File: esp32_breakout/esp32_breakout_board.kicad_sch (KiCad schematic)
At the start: 12 parts, among them U4 ESP32-S3-MINI-1

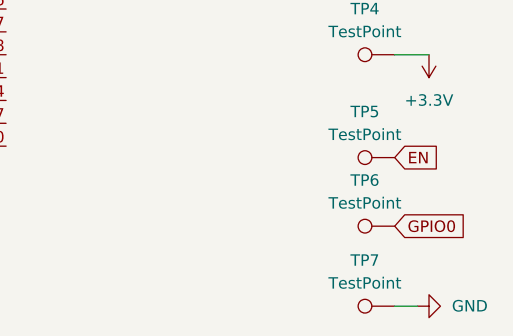
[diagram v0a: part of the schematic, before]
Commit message: Updated esp32 breakout board
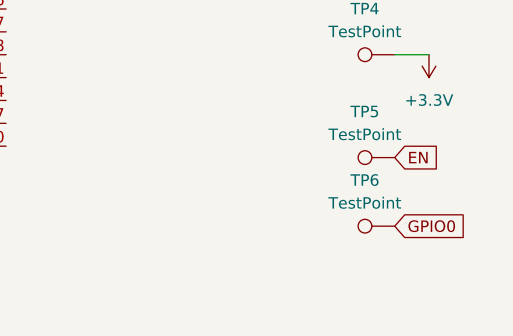
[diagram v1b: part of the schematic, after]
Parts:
- removed TP7: TestPoint, TestPoint:TestPoint_THTPad_D2.0mm_Drill1.0mm, symbol Connector:TestPoint
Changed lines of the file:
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@@
 	(wire
 		(pts
-			(xy 204.47 121.92) (xy 201.93 121.92)
+			(xy 143.51 110.49) (xy 143.51 109.22)
 		)
 		(stroke
@@
 	(wire
 		(pts
-			(xy 143.51 110.49) (xy 143.51 109.22)
+			(xy 205.74 93.98) (xy 201.93 93.98)
 		)
 		(stroke
@@
 	(wire
 		(pts
-			(xy 205.74 93.98) (xy 201.93 93.98)
+			(xy 143.51 44.45) (xy 143.51 48.26)
 		)
 		(stroke
@@
 	(wire
 		(pts
-			(xy 143.51 44.45) (xy 143.51 48.26)
+			(xy 121.92 58.42) (xy 128.27 58.42)
 		)
 		(stroke
@@
 	(wire
 		(pts
-			(xy 121.92 58.42) (xy 128.27 58.42)
+			(xy 55.88 87.63) (xy 71.12 87.63)
 		)
 		(stroke
@@
 	(wire
 		(pts
-			(xy 55.88 87.63) (xy 71.12 87.63)
+			(xy 115.57 58.42) (xy 121.92 58.42)
 		)
 		(stroke
@@
 	(wire
 		(pts
-			(xy 115.57 58.42) (xy 121.92 58.42)
+			(xy 55.88 83.82) (xy 55.88 87.63)
 		)
 		(stroke
@@
 		)
 	)
-	(wire
-		(pts
-			(xy 55.88 83.82) (xy 55.88 87.63)
-		)
-		(stroke
-			(width 0)
-			(type default)
-		)
-	)
 	(global_label "RX"
 		(shape input)
@@
 	)
 	(symbol
-		(lib_id "Connector:TestPoint")
-		(at 201.93 121.92 90)
-		(unit 1)
-		(exclude_from_sim no)
-		(in_bom yes)
-		(on_board yes)
-		(dnp no)
-		(property "Reference" "TP7"
-			(at 198.628 116.84 90)
-			(effects
-				(font
-					(size 1.27 1.27)
-				)
-			)
-		)
-		(property "Value" "TestPoint"
-			(at 198.628 119.38 90)
-			(effects
-				(font
-					(size 1.27 1.27)
-				)
-			)
-		)
-		(property "Footprint" "TestPoint:TestPoint_THTPad_D2.0mm_Drill1.0mm"
-			(at 201.93 116.84 0)
-			(effects
-				(font
-					(size 1.27 1.27)
-				)
-				(hide yes)
-			)
-		)
-		(property "Datasheet" "~"
-			(at 201.93 116.84 0)
-			(effects
-				(font
-					(size 1.27 1.27)
-				)
-				(hide yes)
-			)
-		)
-		(property "Description" "test point"
-			(at 201.93 121.92 0)
-			(effects
-				(font
-					(size 1.27 1.27)
-				)
-				(hide yes)
-			)
-		)
-		(pin "1"
-		)
-		(instances
-			(project "esp32_breakout_board"
-				(path "/6bfc7a3d-a78e-4e3d-b5d4-ec241c5fd7b4"
-					(reference "TP7")
-					(unit 1)
-				)
-			)
-		)
-	)
-	(symbol
 		(lib_id "power:+3.3V")
 		(at 143.51 43.18 0)
@@
 					(unit 1)
 				)
-			)
-		)
-	)
-	(symbol
-		(lib_id "power:GND")
-		(at 204.47 121.92 90)
-		(unit 1)
-		(exclude_from_sim no)
-		(in_bom yes)
-		(on_board yes)
-		(dnp no)
-		(fields_autoplaced yes)
-		(property "Reference" "#PWR09"
-			(at 210.82 121.92 0)
-			(effects
-				(font
-					(size 1.27 1.27)
-				)
-				(hide yes)
-			)
-		)
-		(property "Value" "GND"
-			(at 208.28 121.9199 90)
-			(effects
-				(font
-					(size 1.27 1.27)
-				)
-				(justify right)
-			)
-		)
-		(property "Footprint" ""
-			(at 204.47 121.92 0)
-			(effects
-				(font
-					(size 1.27 1.27)
-				)
-				(hide yes)
-			)
-		)
-		(property "Datasheet" ""
-			(at 204.47 121.92 0)
-			(effects
-				(font
-					(size 1.27 1.27)
-				)
-				(hide yes)
-			)
-		)
-		(property "Description" "Power symbol creates a global label with name \"GND\" , ground"
-			(at 204.47 121.92 0)
-			(effects
-				(font
-					(size 1.27 1.27)
-				)
-				(hide yes)
-			)
-		)
-		(pin "1"
-		)
-		(instances
-			(project "esp32_breakout_board"
-				(path "/6bfc7a3d-a78e-4e3d-b5d4-ec241c5fd7b4"
-					(reference "#PWR09")
-					(unit 1)
-				)
